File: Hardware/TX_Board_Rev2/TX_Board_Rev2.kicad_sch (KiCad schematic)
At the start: 30 parts, among them IC1 GP2Y1+, IC2 GP2Y1+, IC24 ADP5600ACPZ-R7, IC3 GP2Y1+, J1 Conn_Coaxial, J10 MM8030-2610RJ3, J11 MM8030-2610RJ3, J12 MM8030-2610RJ3, J19 694106301002, J8 Conn_02x08_Odd_Even, J9 MM8030-2610RJ3, U1 SN74HCT138NSR

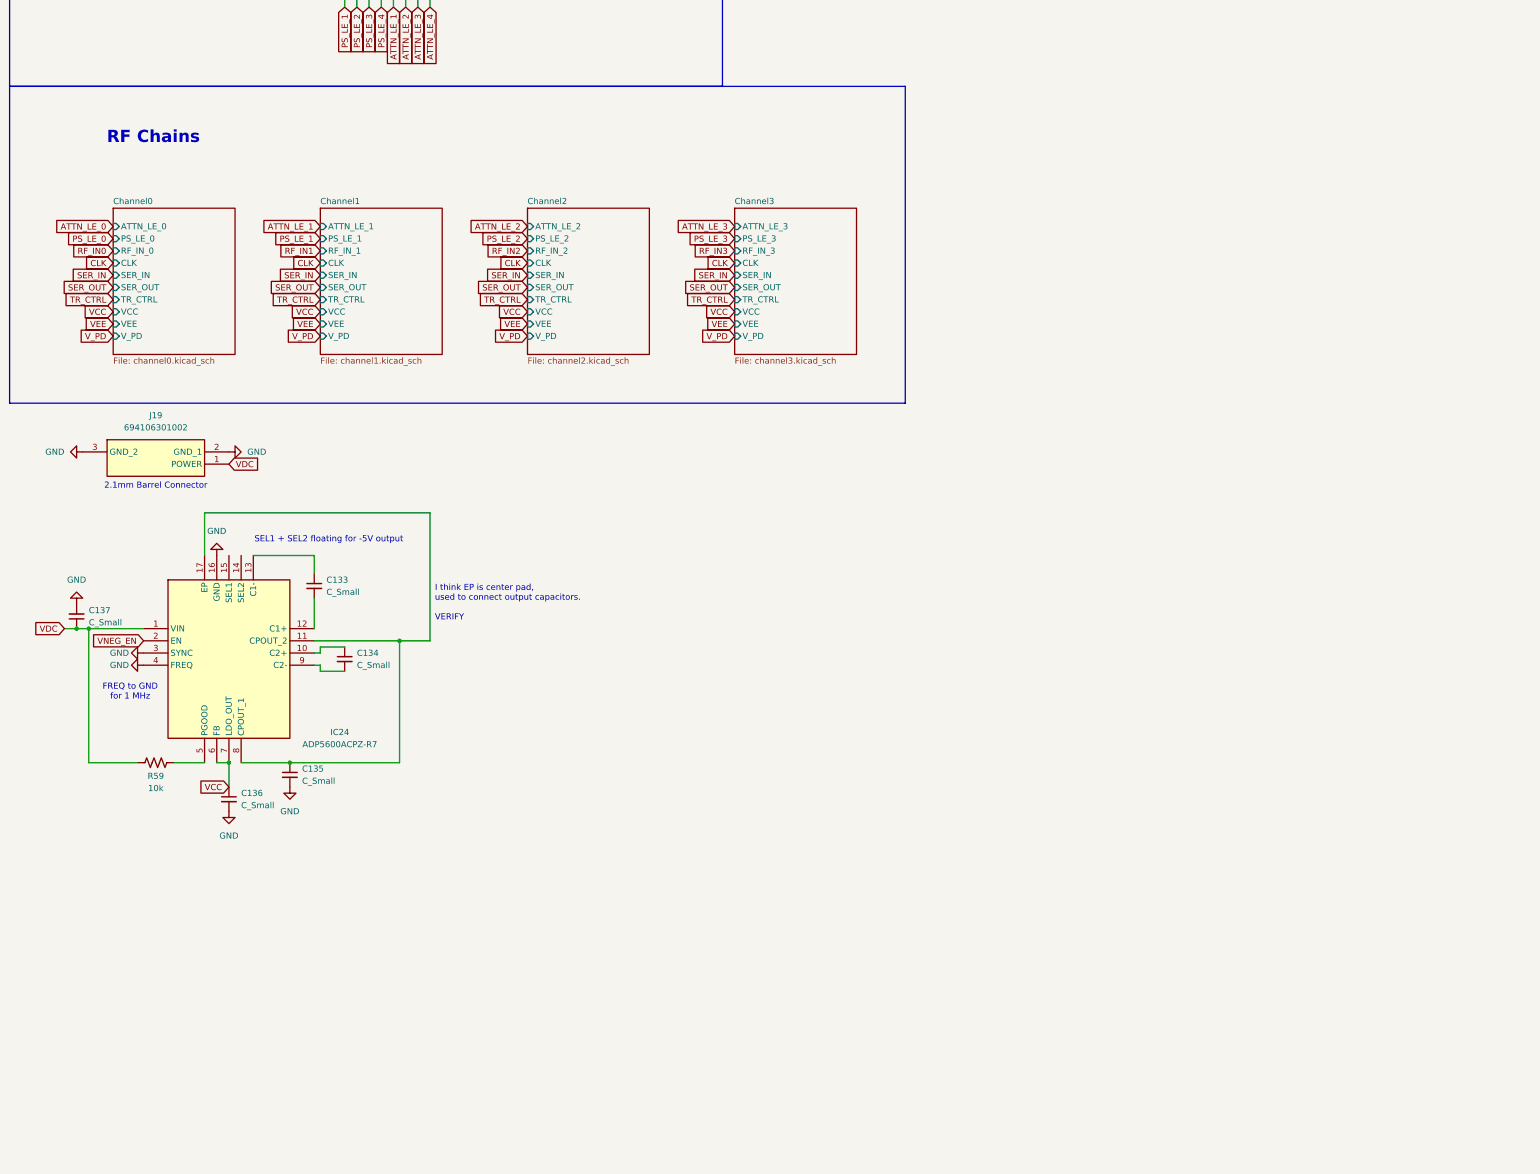
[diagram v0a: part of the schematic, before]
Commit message: Added FT232H ports and positive voltage railto schematic
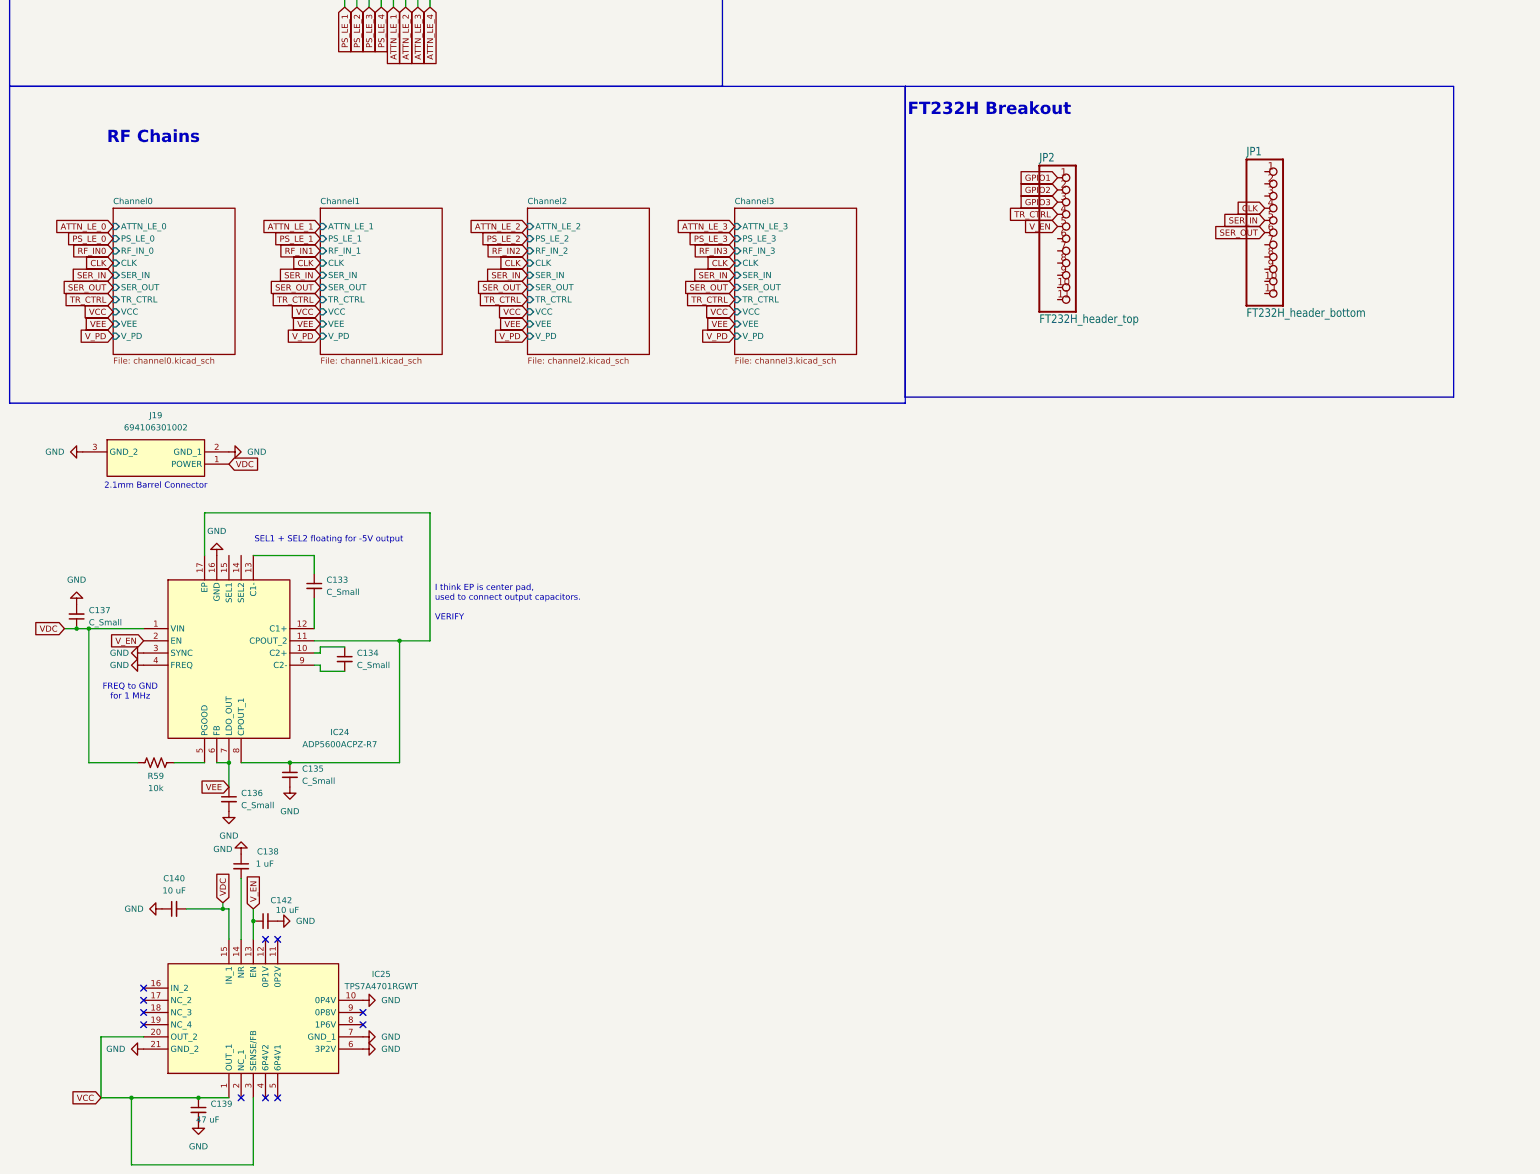
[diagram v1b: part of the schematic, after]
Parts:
- added C138: 1 uF, symbol Device:C_Small
- added C139: 47 uF, symbol Device:C_Small
- added C140, C142: 10 uF, symbol Device:C_Small
- added IC25: TPS7A4701RGWT, QFN65P500X500X100-21N-D, symbol TPS7A4701RGWT:TPS7A4701RGWT
- added JP1: FT232H_header_bottom, ft232h_import:1X11_ROUND, symbol ft232h_import-eagle-import:HEADER-1X11
- added JP2: FT232H_header_top, ft232h_import:1X11_ROUND, symbol ft232h_import-eagle-import:HEADER-1X11
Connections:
- net CLK: now also JP1.4
- net GND: now also C138.1, C139.2, C140.1, C142.2, IC25.10 (0P4V), IC25.21 (GND_2), IC25.6 (3P2V), IC25.7 (GND_1)
- net GPIO1: now also JP2.1
- net GPIO2: now also JP2.2
- net GPIO3: now also JP2.3
- net SER_IN: now also JP1.5
- net SER_OUT: now also JP1.6
- net TR_CTRL: now also JP2.4
- net VCC: now also C139.1, IC25.1 (OUT_1), IC25.20 (OUT_2), IC25.3 (SENSE/FB); no longer C136.1, IC24.6 (FB), IC24.7 (LDO_OUT)
- net VDC: now also C140.2, IC25.15 (IN_1)
- net VEE: now also C136.1, IC24.6 (FB), IC24.7 (LDO_OUT)
- net VNEG_EN renamed V_EN
- net V_EN: now also C142.1, IC25.13 (EN), JP2.5
- new net: C138.2, IC25.14 (NR)
- no-connect marks 0 -> 11
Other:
- note added: "FT232H Breakout"

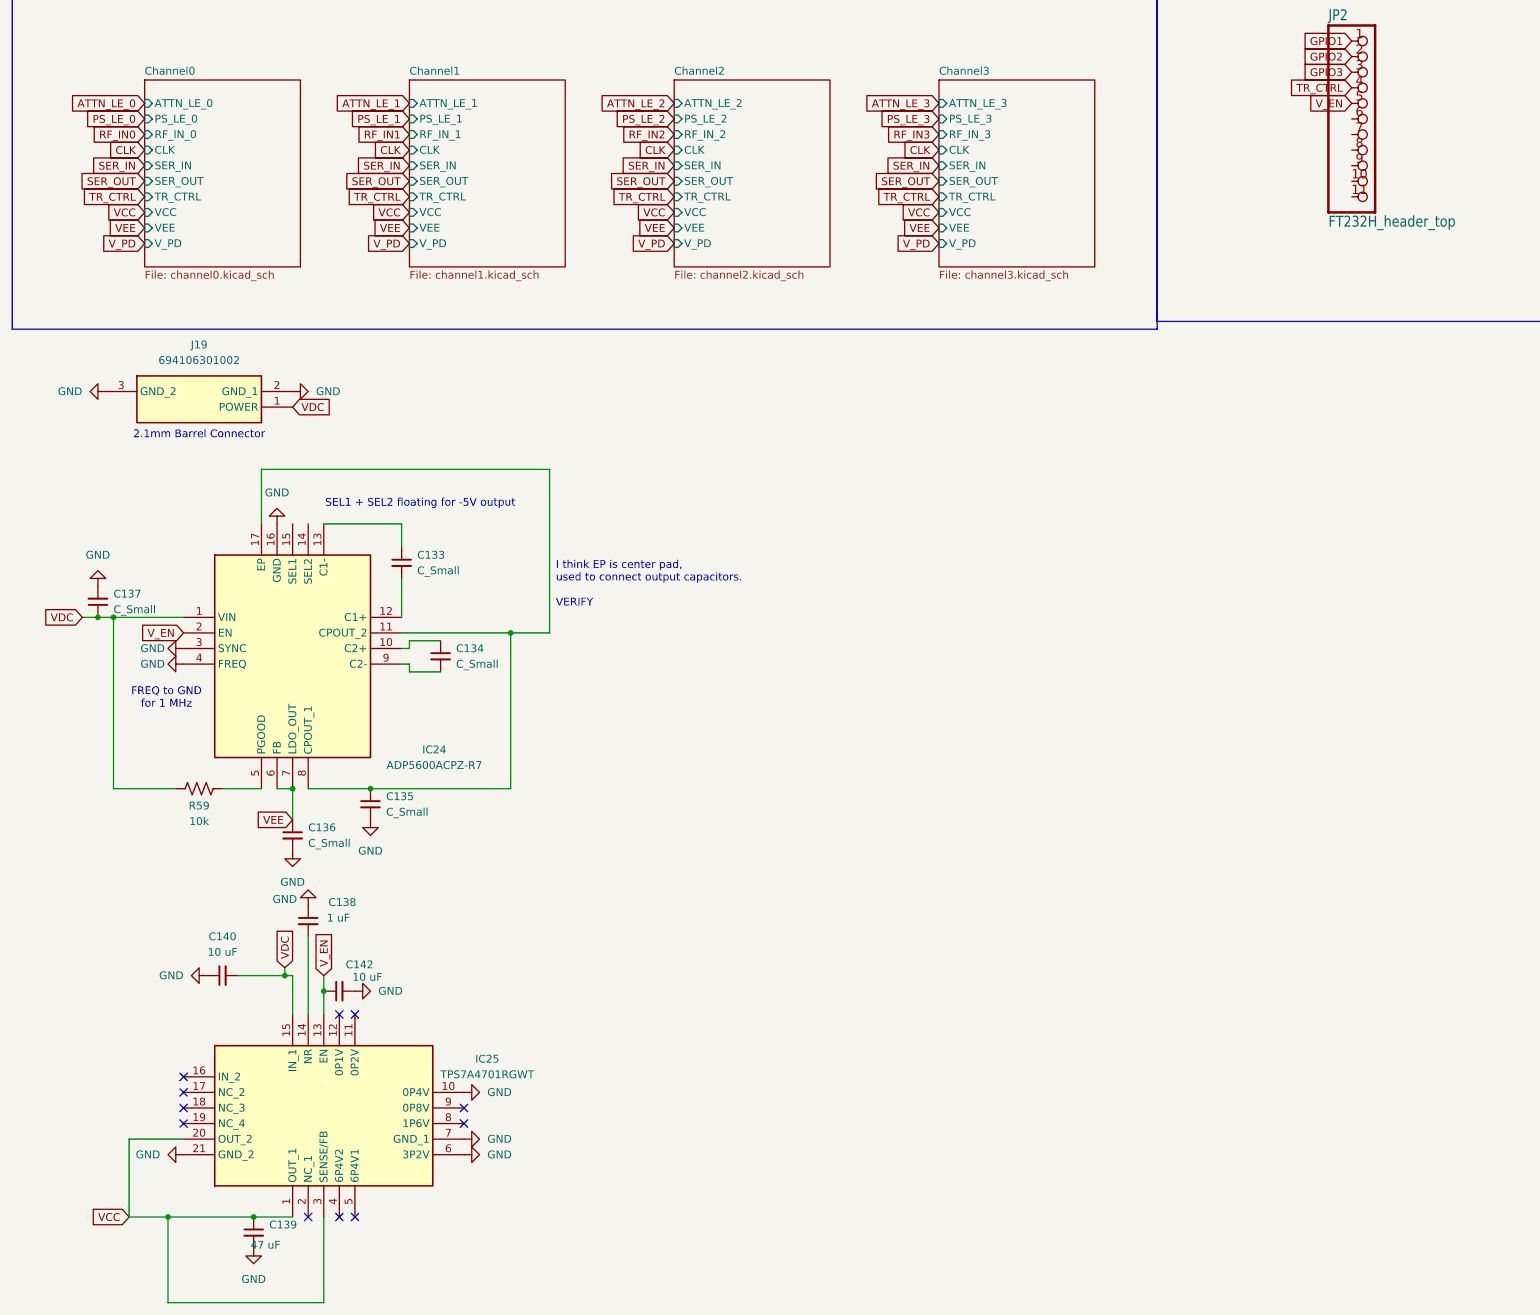
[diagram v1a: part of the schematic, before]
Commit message: adjustments to power and added VPD LDO
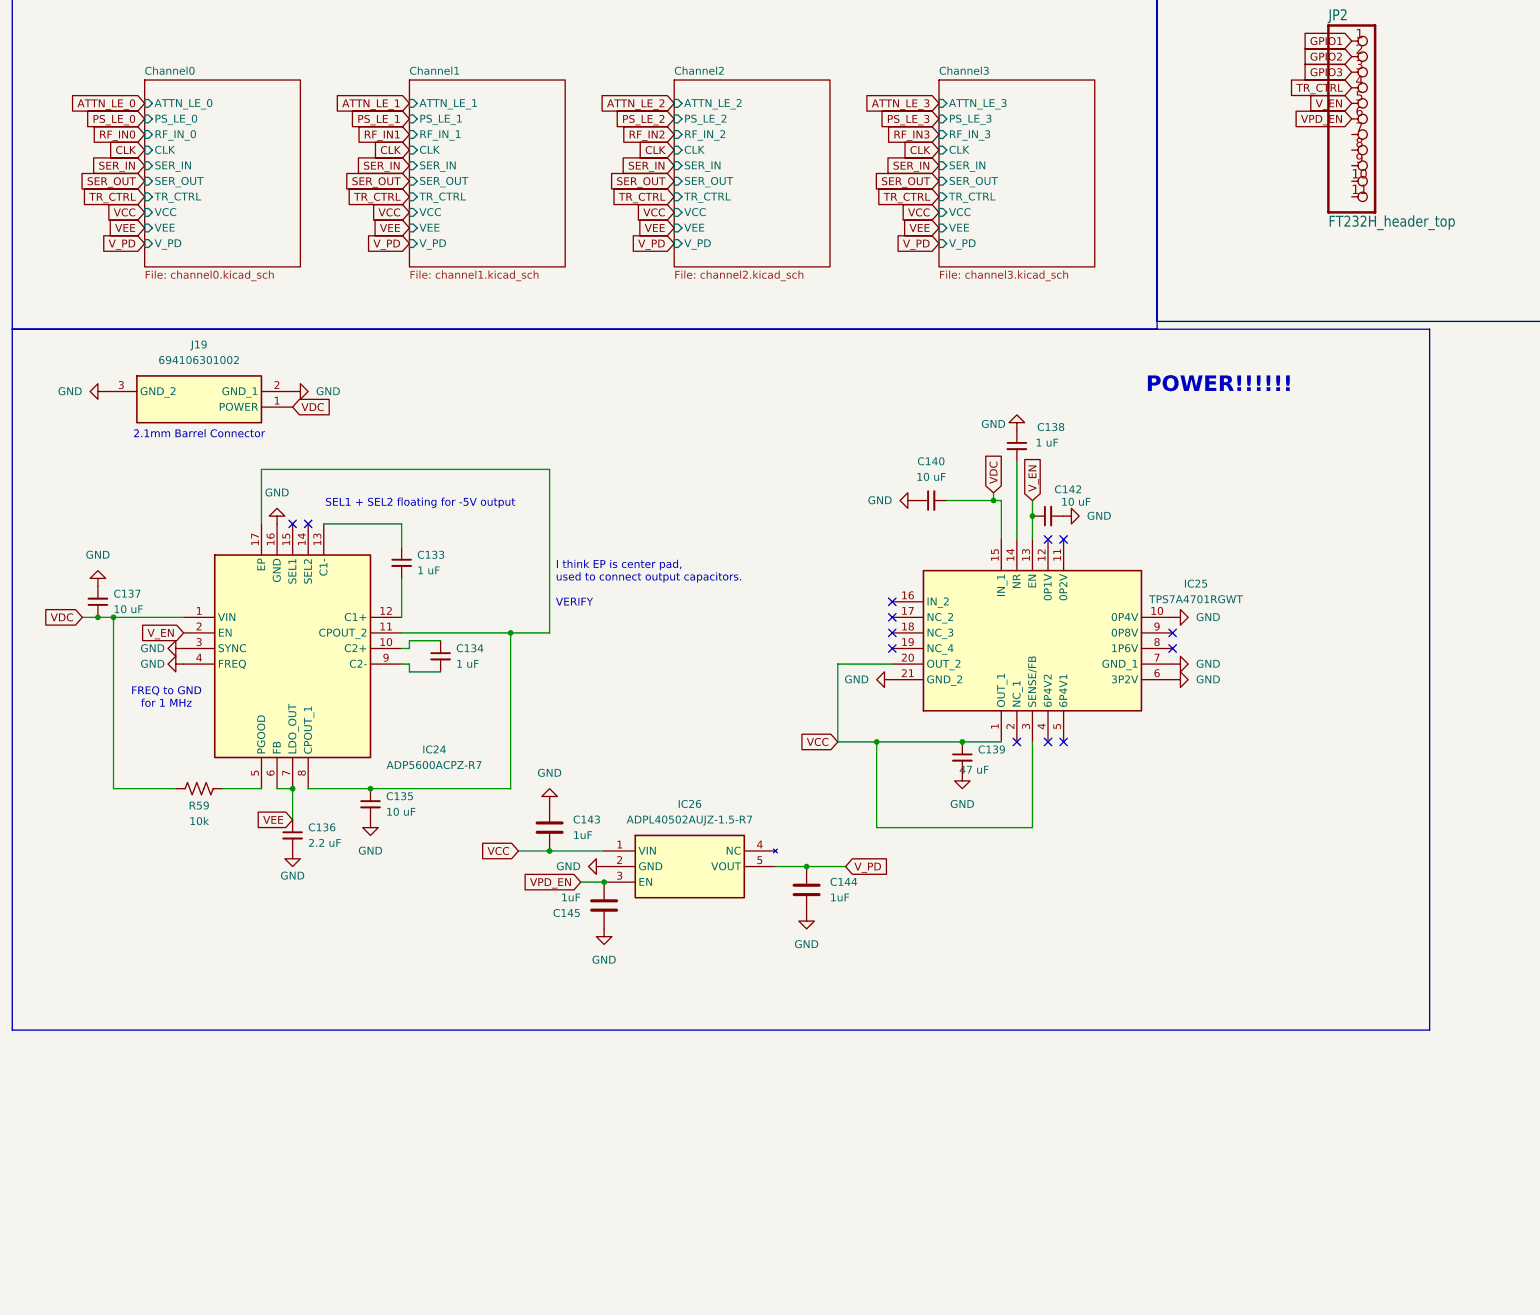
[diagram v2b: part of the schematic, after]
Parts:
- added C143, C144, C145: 1uF, Capacitor_SMD:C_0603_1608Metric, symbol tx_board_symbol_library:C
- added IC26: ADPL40502AUJZ-1.5-R7, tx_board_footprints:SOT95P280X100-5N, symbol tx_board_symbol_library:ADPL40502AUJZ-1.5-R7
- C133, C134: value C_Small -> 1 uF
- C135, C137: value C_Small -> 10 uF
- C136: value C_Small -> 2.2 uF
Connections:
- net GND: now also C143.1, C144.2, C145.1, IC26.2 (GND)
- net VCC: now also C143.2, IC26.1 (VIN)
- net V_PD: now also C144.1, IC26.5 (VOUT)
- net VPD_EN: now reaches JP2.6
- net VPD_EN: now also C145.2, IC26.3 (EN)
- no-connect marks 11 -> 13
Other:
- note added: "POWER!!!!!!"
- moved on the sheet: C138, C139, C140, C142, IC25

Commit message: Rev2 layout partially complete
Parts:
- removed IC26: ADPL40502AUJZ-1.5-R7, tx_board_footprints:SOT95P280X100-5N, symbol tx_board_symbol_library:ADPL40502AUJZ-1.5-R7
- removed J8: Conn_02x08_Odd_Even, Connector_PinHeader_2.54mm:PinHeader_2x08_P2.54mm_Horizontal, symbol tx_board_symbol_library:Conn_02x08_Odd_Even
- added IC27: ADPL40502AUJZ-1.8-R7, ADPL40502AUJZ-1.8-R7:SOT95P280X100-5N, symbol ADPL40502AUJZ-1_8-R7:ADPL40502AUJZ-1.8-R7
- added J20: Conn_01x08, Connector_PinHeader_2.54mm:PinHeader_1x08_P2.54mm_Horizontal, symbol Connector_Generic:Conn_01x08
- C133: footprint (none) -> Capacitor_SMD:C_0402_1005Metric
- C134, C136, C138: footprint (none) -> Capacitor_SMD:C_0603_1608Metric
- C135, C137, C139, C140, C142: footprint (none) -> Capacitor_SMD:C_0805_2012Metric
- C4, C5: footprint Capacitor_SMD:C_0603_1608Metric -> Capacitor_SMD:C_0402_1005Metric
- IC1, IC2, IC3: footprint tx_board_footprints:QFN51P300X300X89-13N -> GP2Y1A+:QFN51P300X300X99-13N
- IC24: footprint QFN65P400X400X80-17N-D -> ADP5600:QFN65P400X400X80-17N-D
- IC25: footprint QFN65P500X500X100-21N-D -> TPS7A4701RGWT:QFN65P500X500X100-21N-D
- J10, J11, J12, J9: footprint tx_board_footprints:MM80302610RJ3 -> MM8030-2610RJ3:MM80302610RJ3
- J19: footprint 694106301002_1 -> 694106301002:694106301002_1
- JP1, JP2: footprint ft232h_import:1X11_ROUND -> Connector_PinHeader_2.54mm:PinHeader_1x11_P2.54mm_Vertical
- R1, R10, R11, R2, R3, R5, R6, R7, R8, R9: footprint Resistor_SMD:R_0603_1608Metric -> Resistor_SMD:R_0402_1005Metric
- R59: footprint (none) -> Resistor_SMD:R_0402_1005Metric
- U1: footprint tx_board_footprints:NS16 -> SN74HCT138NSR:SOIC127P780X200-16N
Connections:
- net ATTN_LE_1: now also J20.4 (Pin_4)
- net ATTN_LE_2: now also J20.3 (Pin_3)
- net ATTN_LE_3: now also J20.2 (Pin_2)
- net ATTN_LE_4: now also J20.1 (Pin_1)
- net GND: now also IC27.2 (GND)
- net PS_LE_1: now also J20.8 (Pin_8)
- net PS_LE_2: now also J20.7 (Pin_7)
- net PS_LE_3: now also J20.6 (Pin_6)
- net PS_LE_4: now also J20.5 (Pin_5)
- net RF_IN0: no longer J10.2 (OUT), J11.2 (OUT), J12.2 (OUT)
- net VCC: now also IC27.1 (VIN)
- net VPD_EN: now also IC27.3 (EN)
- net V_PD: now also IC27.5 (VOUT)
- new net RF_IN1: J10.2 (OUT)
- new net RF_IN2: J11.2 (OUT)
- new net RF_IN3: J12.2 (OUT)
- no-connect marks 13 -> 26
